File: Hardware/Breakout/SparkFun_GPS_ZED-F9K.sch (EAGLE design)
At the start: 82 parts, among them J1 U.FL, J3 QWIIC_RIGHT_ANGLE, J4 QWIIC_RIGHT_ANGLE, U1 UBLOX_ZED_F9R, U2 3.3V, U4 HCPL-270L

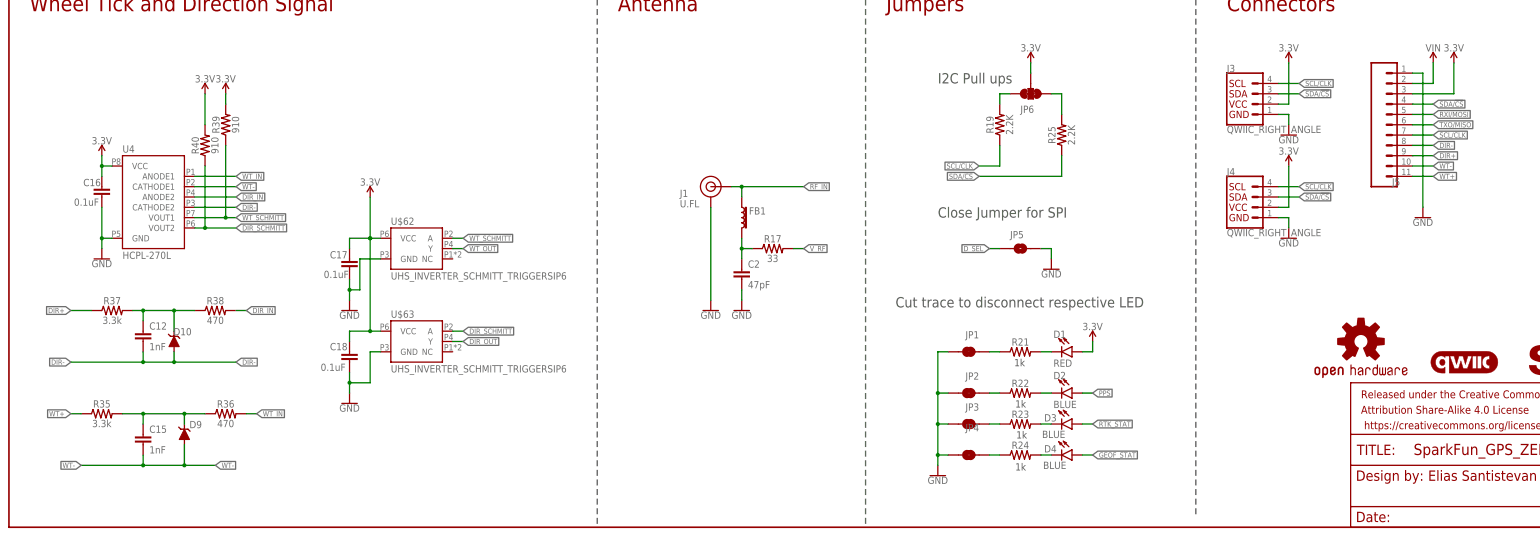
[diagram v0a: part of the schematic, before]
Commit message: Updates wheel tick and direction circuitry with correct grounding
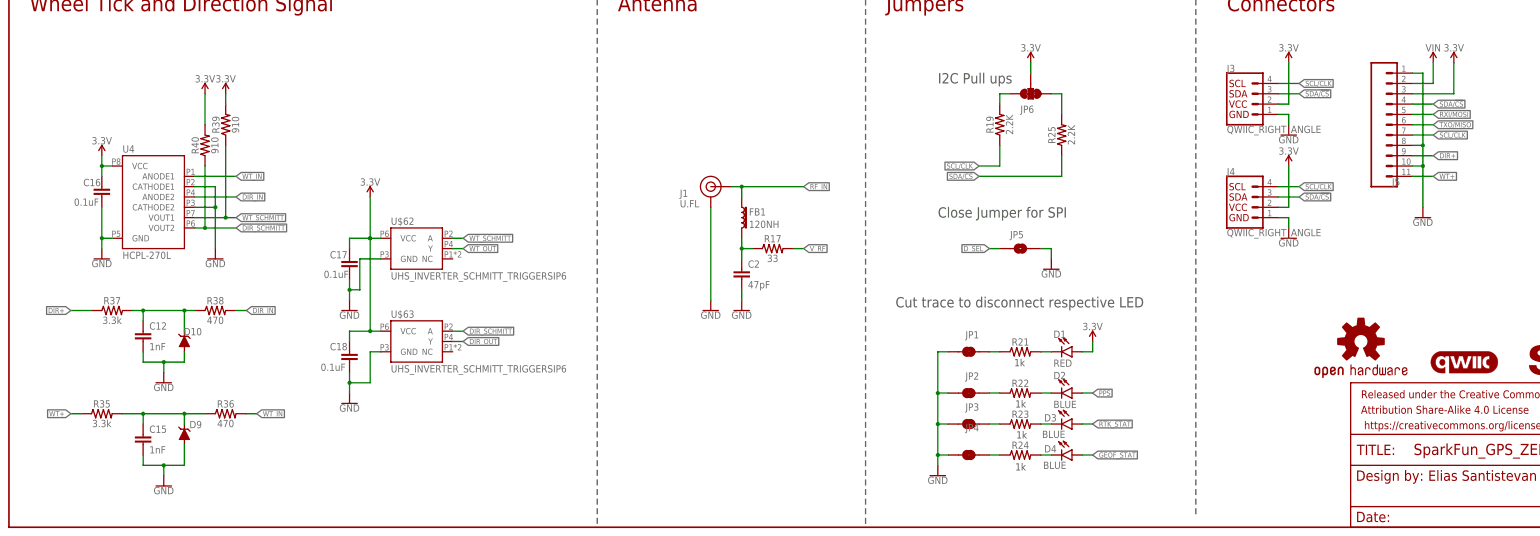
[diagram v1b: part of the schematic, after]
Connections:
- removed net DIR-: C12.2, D10.A, J5.8, U4.CATHODE2
- removed net WT-: C15.2, D9.A, J5.10, U4.CATHODE1
- net GND: now also C12.2, C15.2, D10.A, D9.A, J5.10, J5.8, U4.CATHODE1, U4.CATHODE2
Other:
- moved on the sheet: D10
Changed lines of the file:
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@@
 <part name="C5" library="SparkFun-Capacitors" deviceset="1.0UF" device="-0603-16V-10%-X7R" value="1.0uF"/>
 <part name="GND20" library="SparkFun-PowerSymbols" deviceset="GND" device=""/>
+<part name="GND21" library="SparkFun-PowerSymbols" deviceset="GND" device=""/>
+<part name="GND22" library="SparkFun-PowerSymbols" deviceset="GND" device=""/>
+<part name="GND23" library="SparkFun-PowerSymbols" deviceset="GND" device=""/>
 </parts>
 <sheets>
@@
 </instance>
 <instance part="FB1" gate="G$1" x="180.34" y="76.2" smashed="yes">
-<attribute name="NAME" x="182.118" y="76.962" size="1.778" layer="95" font="vector"/>
+<attribute name="NAME" x="182.118" y="76.708" size="1.778" layer="95" font="vector"/>
+<attribute name="VALUE" x="182.118" y="75.438" size="1.778" layer="96" font="vector" align="top-left"/>
 </instance>
 <instance part="R35" gate="G$1" x="22.86" y="27.94" smashed="yes">
@@
 <attribute name="VALUE" x="83.82" y="30.226" size="1.778" layer="96" align="top-center"/>
 </instance>
-<instance part="D10" gate="G$1" x="40.64" y="45.72" smashed="yes" rot="R90">
-<attribute name="NAME" x="44.958" y="49.022" size="1.778" layer="95" font="vector" rot="R180"/>
+<instance part="D10" gate="G$1" x="43.18" y="45.72" smashed="yes" rot="R90">
+<attribute name="NAME" x="47.498" y="49.022" size="1.778" layer="95" font="vector" rot="R180"/>
 </instance>
 <instance part="SUPPLY23" gate="G$1" x="53.34" y="106.68" smashed="yes">
@@
 <instance part="GND20" gate="1" x="38.1" y="182.88" smashed="yes">
 <attribute name="VALUE" x="38.1" y="182.626" size="1.778" layer="96" align="top-center"/>
+</instance>
+<instance part="GND21" gate="1" x="50.8" y="66.04" smashed="yes">
+<attribute name="VALUE" x="50.8" y="65.786" size="1.778" layer="96" align="top-center"/>
+</instance>
+<instance part="GND22" gate="1" x="38.1" y="35.56" smashed="yes">
+<attribute name="VALUE" x="38.1" y="35.306" size="1.778" layer="96" align="top-center"/>
+</instance>
+<instance part="GND23" gate="1" x="38.1" y="10.16" smashed="yes">
+<attribute name="VALUE" x="38.1" y="9.906" size="1.778" layer="96" align="top-center"/>
 </instance>
 </instances>
@@
 <pinref part="J5" gate="G$1" pin="1"/>
 <wire x1="345.44" y1="111.76" x2="347.98" y2="111.76" width="0.1524" layer="91"/>
-<wire x1="347.98" y1="111.76" x2="347.98" y2="78.74" width="0.1524" layer="91"/>
+<wire x1="347.98" y1="111.76" x2="347.98" y2="93.98" width="0.1524" layer="91"/>
 <pinref part="GND16" gate="1" pin="GND"/>
+<pinref part="J5" gate="G$1" pin="8"/>
+<wire x1="347.98" y1="93.98" x2="347.98" y2="88.9" width="0.1524" layer="91"/>
+<wire x1="347.98" y1="88.9" x2="347.98" y2="78.74" width="0.1524" layer="91"/>
+<wire x1="345.44" y1="93.98" x2="347.98" y2="93.98" width="0.1524" layer="91"/>
+<junction x="347.98" y="93.98"/>
+<pinref part="J5" gate="G$1" pin="10"/>
+<wire x1="345.44" y1="88.9" x2="347.98" y2="88.9" width="0.1524" layer="91"/>
+<junction x="347.98" y="88.9"/>
 </segment>
 <segment>
@@
 <pinref part="GND20" gate="1" pin="GND"/>
 <wire x1="38.1" y1="193.04" x2="38.1" y2="185.42" width="0.1524" layer="91"/>
+</segment>
+<segment>
+<wire x1="33.02" y1="40.64" x2="38.1" y2="40.64" width="0.1524" layer="91"/>
+<wire x1="38.1" y1="40.64" x2="43.18" y2="40.64" width="0.1524" layer="91"/>
+<wire x1="33.02" y1="43.18" x2="33.02" y2="40.64" width="0.1524" layer="91"/>
+<wire x1="43.18" y1="43.18" x2="43.18" y2="40.64" width="0.1524" layer="91"/>
+<pinref part="C12" gate="G$1" pin="2"/>
+<pinref part="D10" gate="G$1" pin="A"/>
+<pinref part="GND22" gate="1" pin="GND"/>
+<wire x1="38.1" y1="38.1" x2="38.1" y2="40.64" width="0.1524" layer="91"/>
+<junction x="38.1" y="40.64"/>
+</segment>
+<segment>
+<wire x1="33.02" y1="17.78" x2="33.02" y2="15.24" width="0.1524" layer="91"/>
+<wire x1="33.02" y1="15.24" x2="38.1" y2="15.24" width="0.1524" layer="91"/>
+<wire x1="38.1" y1="15.24" x2="43.18" y2="15.24" width="0.1524" layer="91"/>
+<wire x1="43.18" y1="20.32" x2="43.18" y2="15.24" width="0.1524" layer="91"/>
+<pinref part="C15" gate="G$1" pin="2"/>
+<pinref part="D9" gate="G$1" pin="A"/>
+<pinref part="GND23" gate="1" pin="GND"/>
+<wire x1="38.1" y1="12.7" x2="38.1" y2="15.24" width="0.1524" layer="91"/>
+<junction x="38.1" y="15.24"/>
+</segment>
+<segment>
+<wire x1="45.72" y1="78.74" x2="50.8" y2="78.74" width="0.1524" layer="91"/>
+<pinref part="U4" gate="G$1" pin="CATHODE2"/>
+<pinref part="GND21" gate="1" pin="GND"/>
+<wire x1="50.8" y1="78.74" x2="50.8" y2="68.58" width="0.1524" layer="91"/>
+<junction x="50.8" y="78.74"/>
+<wire x1="45.72" y1="83.82" x2="50.8" y2="83.82" width="0.1524" layer="91"/>
+<pinref part="U4" gate="G$1" pin="CATHODE1"/>
+<wire x1="50.8" y1="83.82" x2="50.8" y2="78.74" width="0.1524" layer="91"/>
 </segment>
 </net>
@@
 </segment>
 </net>
-<net name="WT-" class="0">
-<segment>
-<wire x1="33.02" y1="17.78" x2="33.02" y2="15.24" width="0.1524" layer="91"/>
-<wire x1="17.78" y1="15.24" x2="33.02" y2="15.24" width="0.1524" layer="91"/>
-<wire x1="33.02" y1="15.24" x2="43.18" y2="15.24" width="0.1524" layer="91"/>
-<junction x="33.02" y="15.24"/>
-<wire x1="43.18" y1="20.32" x2="43.18" y2="15.24" width="0.1524" layer="91"/>
-<wire x1="43.18" y1="15.24" x2="50.8" y2="15.24" width="0.1524" layer="91"/>
-<junction x="43.18" y="15.24"/>
-<label x="17.78" y="15.24" size="1.27" layer="95" font="vector" rot="R180" xref="yes"/>
-<label x="50.8" y="15.24" size="1.27" layer="95" font="vector" xref="yes"/>
-<pinref part="C15" gate="G$1" pin="2"/>
-<pinref part="D9" gate="G$1" pin="A"/>
-</segment>
-<segment>
-<wire x1="45.72" y1="83.82" x2="55.88" y2="83.82" width="0.1524" layer="91"/>
-<label x="55.88" y="83.82" size="1.27" layer="95" font="vector" xref="yes"/>
-<pinref part="U4" gate="G$1" pin="CATHODE1"/>
-</segment>
-<segment>
-<pinref part="J5" gate="G$1" pin="10"/>
-<wire x1="345.44" y1="88.9" x2="350.52" y2="88.9" width="0.1524" layer="91"/>
-<label x="350.52" y="88.9" size="1.27" layer="95" xref="yes"/>
-</segment>
-</net>
 <net name="WT+" class="0">
 <segment>
@@
 </segment>
 </net>
-<net name="DIR-" class="0">
-<segment>
-<wire x1="15.24" y1="40.64" x2="33.02" y2="40.64" width="0.1524" layer="91"/>
-<wire x1="33.02" y1="40.64" x2="40.64" y2="40.64" width="0.1524" layer="91"/>
-<wire x1="40.64" y1="40.64" x2="55.88" y2="40.64" width="0.1524" layer="91"/>
-<wire x1="33.02" y1="43.18" x2="33.02" y2="40.64" width="0.1524" layer="91"/>
-<junction x="33.02" y="40.64"/>
-<wire x1="40.64" y1="43.18" x2="40.64" y2="40.64" width="0.1524" layer="91"/>
-<junction x="40.64" y="40.64"/>
-<label x="15.24" y="40.64" size="1.27" layer="95" font="vector" rot="R180" xref="yes"/>
-<label x="55.88" y="40.64" size="1.27" layer="95" font="vector" xref="yes"/>
-<pinref part="C12" gate="G$1" pin="2"/>
-<pinref part="D10" gate="G$1" pin="A"/>
-</segment>
-<segment>
-<wire x1="45.72" y1="78.74" x2="55.88" y2="78.74" width="0.1524" layer="91"/>
-<label x="55.88" y="78.74" size="1.27" layer="95" font="vector" xref="yes"/>
-<pinref part="U4" gate="G$1" pin="CATHODE2"/>
-</segment>
-<segment>
-<pinref part="J5" gate="G$1" pin="8"/>
-<wire x1="345.44" y1="93.98" x2="350.52" y2="93.98" width="0.1524" layer="91"/>
-<label x="350.52" y="93.98" size="1.27" layer="95" font="vector" xref="yes"/>
-</segment>
-</net>
 <net name="DIR+" class="0">
 <segment>
@@
 <segment>
 <wire x1="30.48" y1="53.34" x2="33.02" y2="53.34" width="0.1524" layer="91"/>
-<wire x1="33.02" y1="53.34" x2="40.64" y2="53.34" width="0.1524" layer="91"/>
-<wire x1="40.64" y1="53.34" x2="45.72" y2="53.34" width="0.1524" layer="91"/>
+<wire x1="33.02" y1="53.34" x2="43.18" y2="53.34" width="0.1524" layer="91"/>
+<wire x1="43.18" y1="53.34" x2="45.72" y2="53.34" width="0.1524" layer="91"/>
 <wire x1="33.02" y1="50.8" x2="33.02" y2="53.34" width="0.1524" layer="91"/>
 <junction x="33.02" y="53.34"/>
-<wire x1="40.64" y1="48.26" x2="40.64" y2="53.34" width="0.1524" layer="91"/>
-<junction x="40.64" y="53.34"/>
+<wire x1="43.18" y1="48.26" x2="43.18" y2="53.34" width="0.1524" layer="91"/>
+<junction x="43.18" y="53.34"/>
 <pinref part="R37" gate="G$1" pin="2"/>
 <pinref part="R38" gate="G$1" pin="1"/>
